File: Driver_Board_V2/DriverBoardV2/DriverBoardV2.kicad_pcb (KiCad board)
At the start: 2 copper layers, 77.2 x 116 mm, 29 parts, among them IC1 L7805ABV, J1 ESC1_PWR, J10 M1_OUT, J2 ESC2_PWR, J3 IO_HEADER_1, J4 BATTERY, J5 M2_IN, J6 M2_OUT, J7 IO_HEADER_2, J8 EXT +5V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

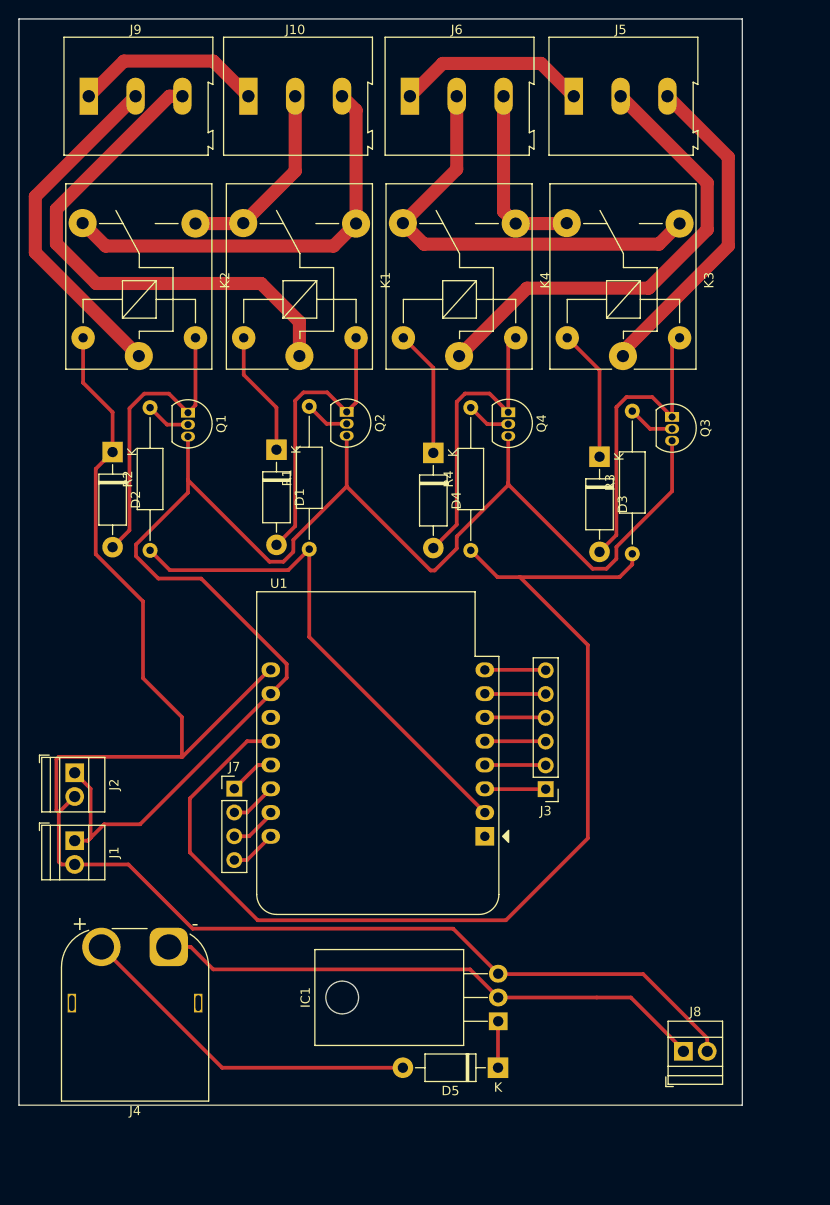
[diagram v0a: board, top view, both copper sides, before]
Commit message: Updated schematic due to layout consideration and increase 5V rail track sizes
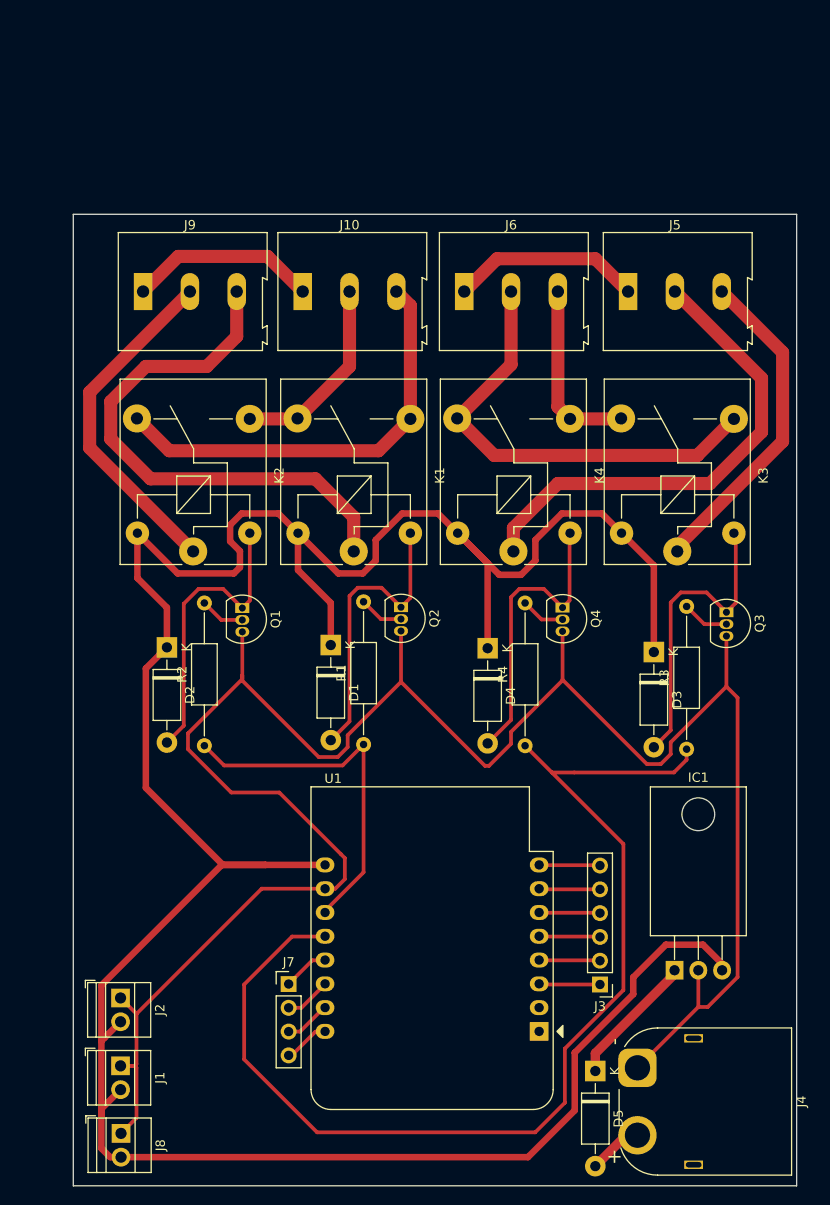
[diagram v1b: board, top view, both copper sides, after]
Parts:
- moved J8 60.7 mm to (122.7, 141.5), turned to -90 degrees
- moved J4 51.7 mm to (177.8, 134.5), turned to -90 degrees
- moved J1 24.5 mm to (122.6, 134.3)
- moved J2 24.5 mm to (122.6, 127.0)
- moved D1 21.7 mm to (145.1, 89.4)
- moved D3 21.7 mm to (179.6, 90.1)
- moved D4 21.7 mm to (161.8, 89.7)
- moved J10 21.7 mm to (142.1, 51.6)
- moved J3 21.7 mm to (173.8, 125.6)
- moved J5 21.7 mm to (176.8, 51.6)
- moved J6 21.7 mm to (159.3, 51.6)
- moved J7 21.7 mm to (140.6, 125.6)
- moved K1 21.7 mm to (147.5, 79.4)
- moved K3 21.7 mm to (182.1, 79.4)
- moved K4 21.7 mm to (164.6, 79.4)
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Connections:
- U1 pad 11: unconnected-(U1-D4-Pad11) -> dOUT_MOTOR1_DIR
- U1 pad 2: dOUT_MOTOR1_DIR -> unconnected-(U1-A0-Pad2)
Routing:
- net +5V: track 210.5 -> 296.8 mm
- net +BATT: track 37.5 -> 4.67 mm
- net dOUT_MOTOR1_DIR: track 54.7 -> 38.4 mm
- net Net-(D5-K): track 4.97 -> 14.3 mm
- net M1_ESC_CONTROL_1: track 55.2 -> 58.2 mm
- net M2_ESC_CONTROL_2: track 50.2 -> 52.1 mm
- net dOUT_MOTOR2_DIR: track 117.1 -> 118.7 mm
- net MOTOR2_POLE2: track 47.3 -> 48.7 mm
- net GND: track 226.8 -> 228.0 mm
- net MOTOR1_POLE2: track 45.4 -> 46.3 mm
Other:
- board size 77.2 x 116 mm -> 77.3 x 103.8 mm
